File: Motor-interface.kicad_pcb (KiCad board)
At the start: 2 copper layers, 100.3 x 110.5 mm, 70 parts, among them J101 0, J102 0, J201 RJ45, J202 RJ45, P101 TE-23pins connector, P102 PSU_ISO, P103 Halls, P104 LineContactor, P105 ReverseContactor, P106 FanContactor, P107 Battery+, P108 MC_USB, P109 MC_CAN, Q101 Q_NPN_BCE, U101 AP1117D50, U102 AP1117D33, U103 TLP2361, U104 TLP2361, U105 TLP2361, U106 TLP2361, U107 TLP2361, U108 TLP2361, U109 Teensy_3.2, U110 TLP2361, U111 FODM3052, U201 TLP2361, U202 TLP2361, U203 MCP2551-I/SN, U301 MCP4251, U302 TLP2361, U303 TLP2361, U304 TLP2361, U305 TLP2361, U306 TLP290-4

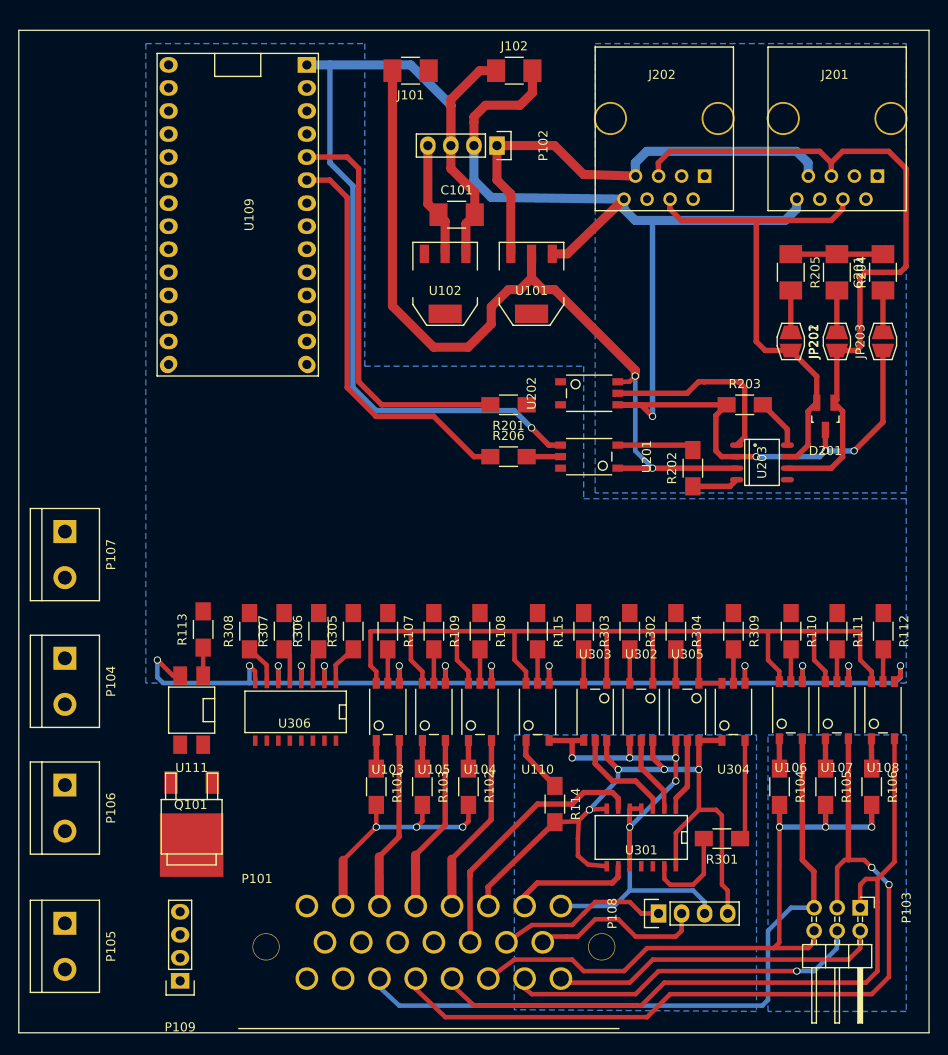
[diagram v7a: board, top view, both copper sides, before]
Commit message: laid out Contactors and monitors
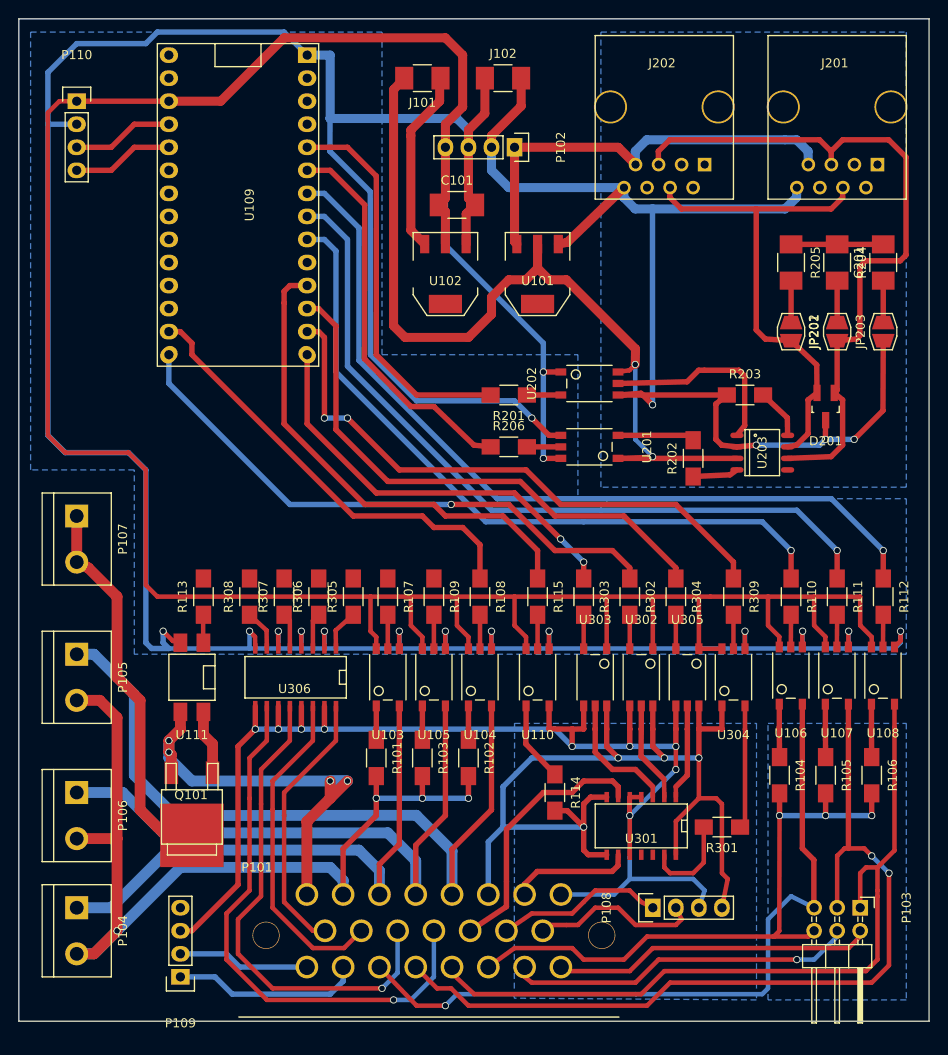
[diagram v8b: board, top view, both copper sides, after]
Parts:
- added P110: HallCurrent, Pin_Headers:Pin_Header_Straight_1x04, F.Cu at (49.6, 70.0)
- moved P105 29.7 mm to (49.6, 133.5)
- moved P104 27.5 mm to (49.6, 161.5)
- moved R107 3.81 mm to (83.8, 124.7)
- moved R108 3.81 mm to (94.0, 124.7)
- moved R109 3.81 mm to (88.9, 124.7)
- moved R110 3.81 mm to (128.3, 124.7)
- moved R111 3.81 mm to (133.4, 124.7)
- moved R112 3.81 mm to (138.5, 124.7)
- moved R115 3.81 mm to (100.4, 124.7)
- moved R302 3.81 mm to (110.5, 124.7)
- moved R303 3.81 mm to (105.4, 124.7)
- moved R304 3.81 mm to (115.6, 124.7)
- moved R305 3.81 mm to (80.0, 124.7)
- moved R306 3.81 mm to (76.2, 124.7)
- moved R307 3.81 mm to (72.4, 124.7)
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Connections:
- net Net-(P107-Pad1) renamed /Battery+
- net Net-(Q101-Pad1) renamed /on_triac
- J201 pad 1: Net-(J201-Pad1) -> (no net)
- J201 pad 2: Net-(J201-Pad2) -> (no net)
- J201 pad 3: Net-(J201-Pad3) -> (no net)
- J201 pad 6: Net-(J201-Pad6) -> (no net)
- J202 pad 1: Net-(J202-Pad1) -> (no net)
- J202 pad 2: Net-(J202-Pad2) -> (no net)
- J202 pad 3: Net-(J202-Pad3) -> (no net)
- J202 pad 6: Net-(J202-Pad6) -> (no net)
- P109 pad 1: /Motor_CAN-H -> /Motor_CAN-L
- P109 pad 2: /Motor_CAN-L -> /Motor_CAN-H
- U109 pad 10: /PotsSwitches/Hybrid -> (no net)
- U109 pad 11: /MOT_ON -> /Motor_Logic_On
- U109 pad 16: Net-(U109-Pad16) -> /Rev-Cont
- U109 pad 17: Net-(U109-Pad17) -> /Fan_Cont
- U109 pad 18: Net-(U109-Pad18) -> /Line-Cont
- U109 pad 19: /Fan_Cont -> /PotsSwitches/Reverse
- U109 pad 2: Net-(U109-Pad2) -> (no net)
- U109 pad 20: /Rev-Cont -> /PotsSwitches/Brake
- U109 pad 21: /Line-Cont -> /PotsSwitches/Cruise
- U109 pad 22: /HallA -> /PotsSwitches/Hybrid
- U109 pad 23: /HallB -> /MOT_ON
- U109 pad 24: /HallC -> /I_Hall
- U109 pad 25: /Motor_Logic_On -> /I_HallRef
- U109 pad 27: Net-(U109-Pad27) -> (no net)
- U109 pad 28: Net-(U109-Pad28) -> (no net)
- U109 pad 3: Net-(U109-Pad3) -> (no net)
- U109 pad 4: Net-(U109-Pad4) -> (no net)
- U109 pad 7: /PotsSwitches/Reverse -> /HallC
- U109 pad 8: /PotsSwitches/Brake -> /HallB
- U109 pad 9: /PotsSwitches/Cruise -> /HallA
- U203 pad 5: Net-(U203-Pad5) -> (no net)
- U301 pad 11: Net-(U301-Pad11) -> (no net)
- U301 pad 12: Net-(U301-Pad12) -> (no net)
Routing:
- net +3V3: track 129.5 -> 317.5 mm, vias 0 -> 2
- net GND: track 242.0 -> 346.1 mm
- net /HallC: track 0.00 -> 91.4 mm, vias 0 -> 1
- net /HallB: track 0.00 -> 84.9 mm, vias 0 -> 1
- net /PotsSwitches/Motor_GND: track 65.8 -> 149.0 mm, vias 5 -> 9
- net /HallA: track 0.00 -> 78.4 mm, vias 0 -> 1
- net /Contactor+Common: track 27.6 -> 103.7 mm, vias 3 -> 4
- net /PotsSwitches/MISO: track 0.00 -> 64.5 mm, vias 0 -> 2
- net /PotsSwitches/SCK: track 0.00 -> 63.6 mm, vias 0 -> 1
- net /Reverse-contactor-coil: track 20.1 -> 83.0 mm
- net /PotsSwitches/Hybrid-Switch: track 0.00 -> 60.6 mm, vias 0 -> 1
- net /PotsSwitches/DP-CS: track 0.00 -> 60.3 mm
- net /Motor_Logic_On: track 0.00 -> 54.2 mm
- net /PotsSwitches/Cruise-Switch: track 0.00 -> 54.2 mm, vias 0 -> 1
- net /Rev-Cont: track 0.00 -> 48.5 mm
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- added copper zone on B.Cu, net /PotsSwitches/Motor_GND
- removed copper zone on B.Cu, net /M_GND
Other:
- net class Default: trace_width 0.25 -> 0.5
- net class HT added: clearance 0.6, trace_width 0.6, via_dia 0.6, via_drill 0.4
